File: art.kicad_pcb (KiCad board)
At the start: 2 copper layers, 43.2 x 43.2 mm, 3 parts

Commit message: update
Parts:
- removed ? (x2): , label
- removed the REF** at (132.2, 106.6)
- added REF**: OSHW-Logo2_36.5x30mm_Copper, Symbol:OSHW-Logo2_36.5x30mm_Copper, F.Cu at (0.05, 210.0)
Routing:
- removed copper zone on F.Cu, net (none)
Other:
- board outline removed
- board text removed: "CU TEST"
- board text removed: "MASK TEST"
- board text removed: "SILK TEST"

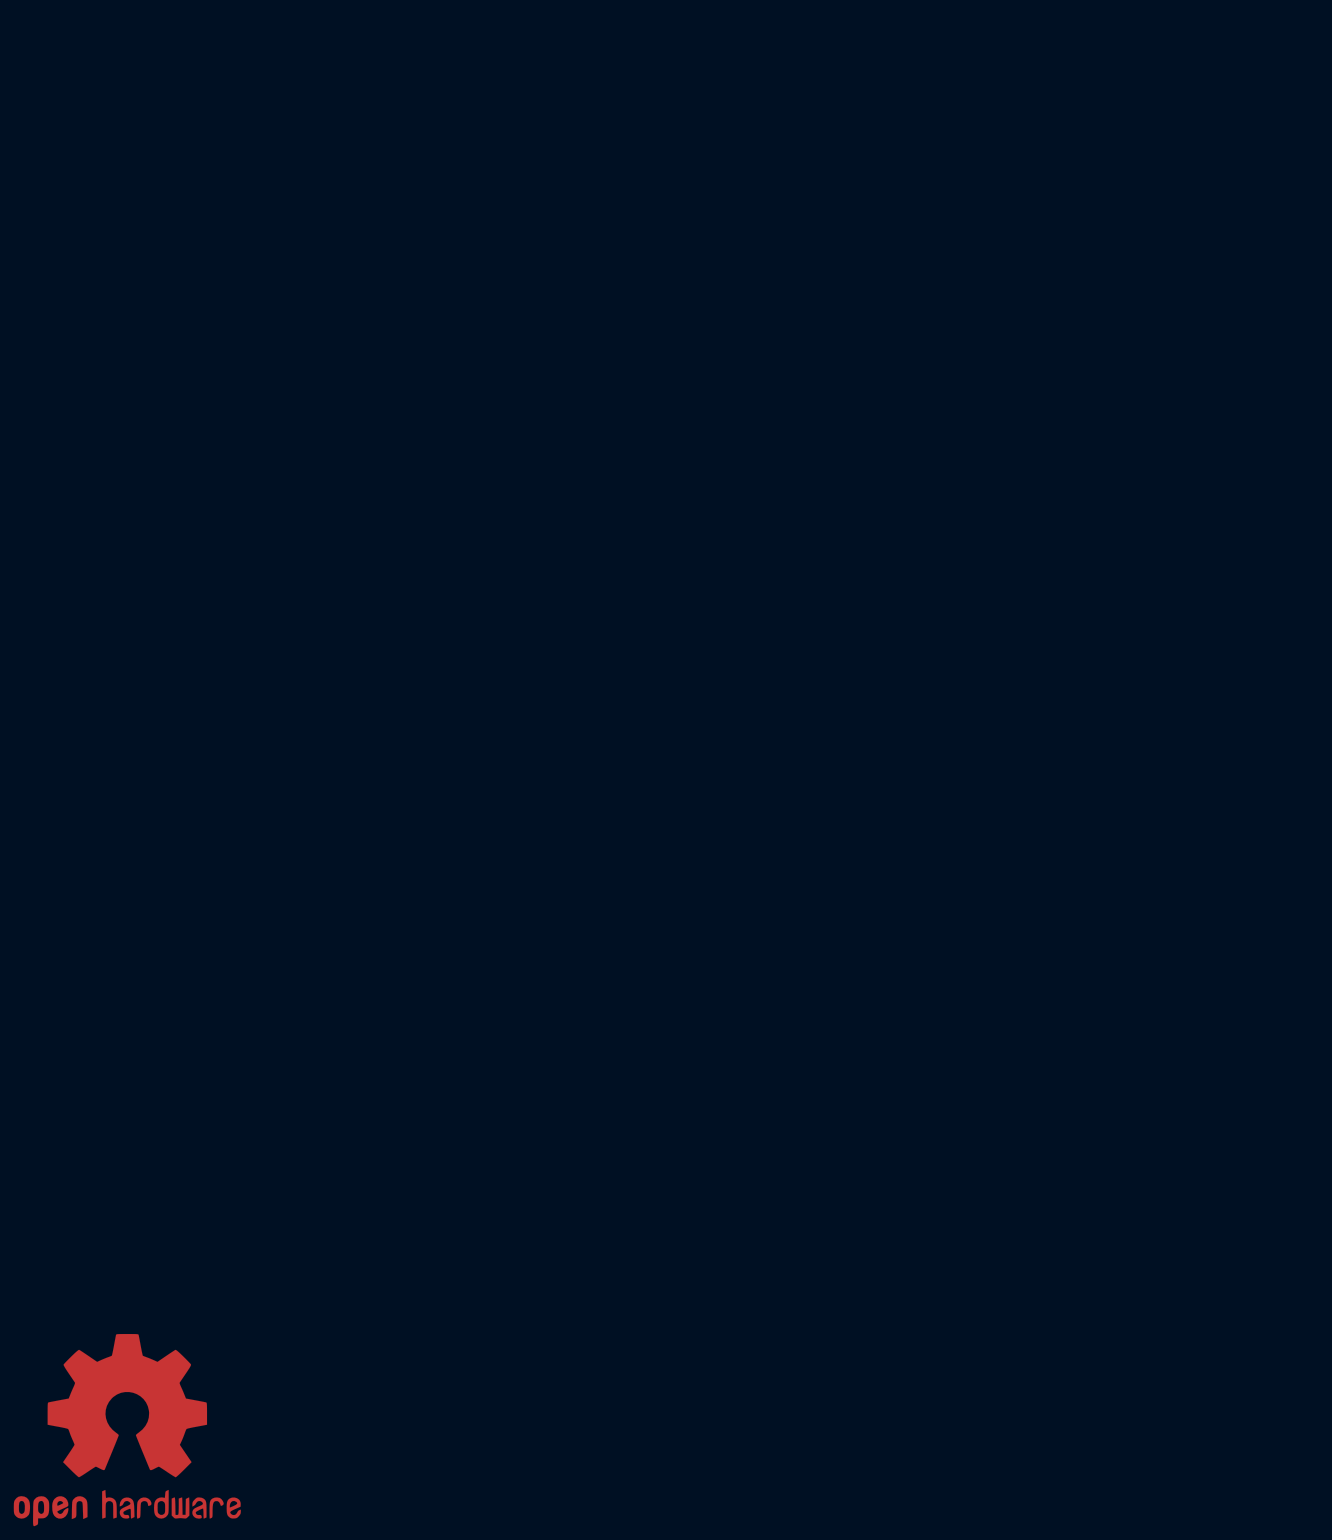
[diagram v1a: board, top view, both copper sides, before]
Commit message: add cutout test
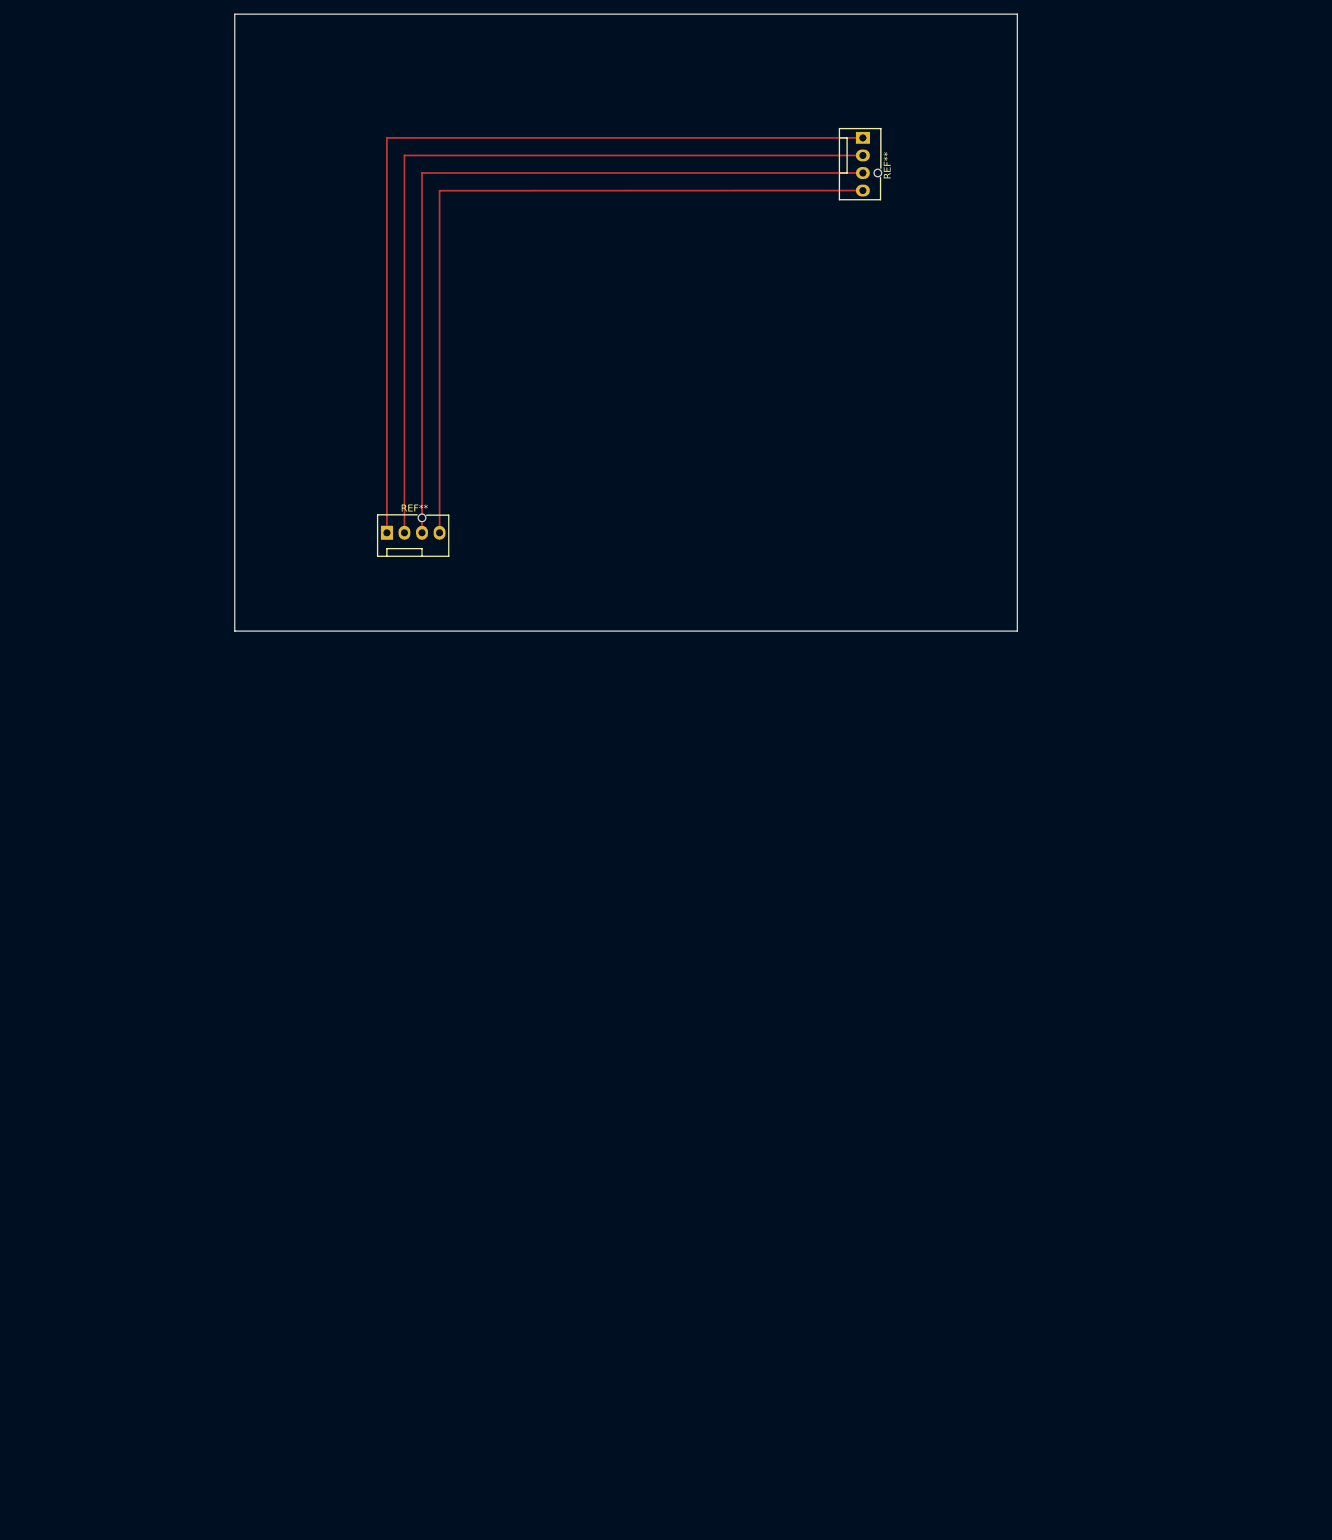
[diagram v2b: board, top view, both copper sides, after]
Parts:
- removed the REF** at (0.05, 210.0)
- added REF**: FanPinHeader_1x04_P2.54mm_Vertical, Connector:FanPinHeader_1x04_P2.54mm_Vertical, F.Cu at (106.5, 23.0)
- added REF**: FanPinHeader_1x04_P2.54mm_Vertical, Connector:FanPinHeader_1x04_P2.54mm_Vertical, F.Cu at (37.6, 80.2)
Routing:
- net (no net): track 0.00 -> 473.8 mm
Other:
- board outline added: 113.3 x 89.3 mm
